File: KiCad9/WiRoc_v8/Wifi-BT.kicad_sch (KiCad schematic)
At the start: 1 part, among them U19 ESP32-C5-Board

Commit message: etc
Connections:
- net VDD_SYS_3.3V: now also U19.10 (VDD33); no longer U19.1 (VDD33)
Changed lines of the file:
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@@
-	)
-	(no_connect
-		(at 161.29 82.55)
 	)
 	(no_connect
 		(at 137.16 82.55)
+	)
+	(no_connect
+		(at 137.16 80.01)
 	)
 	(global_label "WIFI-SPI-CS0"
@@
 	(global_label "VDD_SYS_3.3V"
 		(shape input)
-		(at 137.16 80.01 180)
+		(at 161.29 82.55 0)
 		(fields_autoplaced yes)
 		(effects
@@
 				(size 1.524 1.524)
 			)
-			(justify right)
+			(justify left)
 		)
 		(property "Intersheetrefs" "${INTERSHEET_REFS}"
-			(at 118.5428 80.01 0)
+			(at 179.9072 82.55 0)
 			(effects
 				(font
 					(size 1.27 1.27)
 				)
-				(justify right)
+				(justify left)
 				(hide yes)
 			)

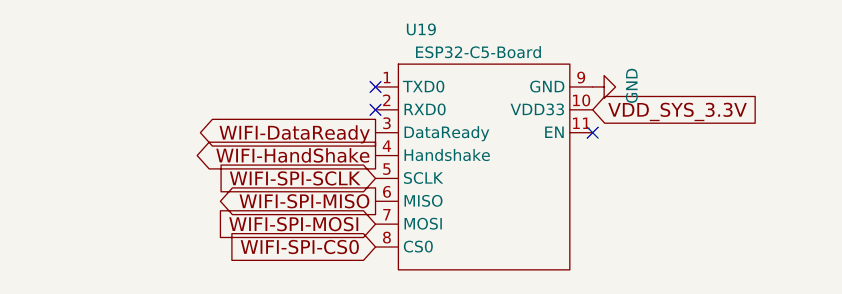
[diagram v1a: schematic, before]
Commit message: more routing of WiRoc_v8, upgraded USBConnectorPlate to v9 and with ferrit beads, added an ESPHosted testboard
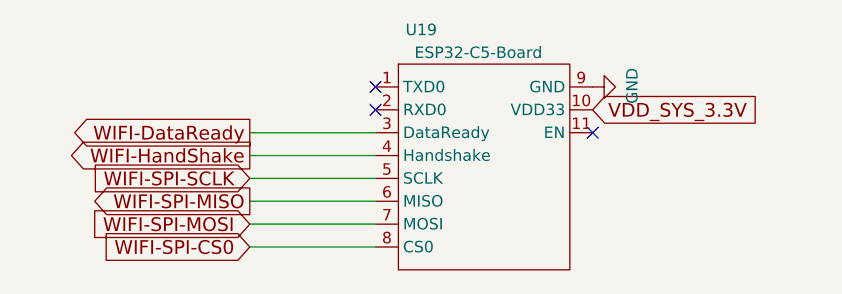
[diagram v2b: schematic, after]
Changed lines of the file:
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@@
 		(at 137.16 80.01)
 	)
+	(wire
+		(pts
+			(xy 123.19 92.71) (xy 137.16 92.71)
+		)
+		(stroke
+			(width 0)
+			(type default)
+		)
+	)
+	(wire
+		(pts
+			(xy 123.19 90.17) (xy 137.16 90.17)
+		)
+		(stroke
+			(width 0)
+			(type default)
+		)
+	)
+	(wire
+		(pts
+			(xy 123.19 87.63) (xy 137.16 87.63)
+		)
+		(stroke
+			(width 0)
+			(type default)
+		)
+	)
+	(wire
+		(pts
+			(xy 123.19 85.09) (xy 137.16 85.09)
+		)
+		(stroke
+			(width 0)
+			(type default)
+		)
+	)
+	(wire
+		(pts
+			(xy 123.19 97.79) (xy 137.16 97.79)
+		)
+		(stroke
+			(width 0)
+			(type default)
+		)
+	)
+	(wire
+		(pts
+			(xy 123.19 95.25) (xy 137.16 95.25)
+		)
+		(stroke
+			(width 0)
+			(type default)
+		)
+	)
 	(global_label "WIFI-SPI-CS0"
 		(shape input)
-		(at 137.16 97.79 180)
-		(fields_autoplaced yes)
-		(effects
-			(font
-				(size 1.524 1.524)
-			)
-			(justify right)
-		)
-		(property "Intersheetrefs" "${INTERSHEET_REFS}"
-			(at 117.9621 97.79 0)
+		(at 123.19 97.79 180)
+		(fields_autoplaced yes)
+		(effects
+			(font
+				(size 1.524 1.524)
+			)
+			(justify right)
+		)
+		(property "Intersheetrefs" "${INTERSHEET_REFS}"
+			(at 103.9921 97.79 0)
 			(effects
 				(font
@@
 	(global_label "WIFI-DataReady"
 		(shape output)
-		(at 137.16 85.09 180)
-		(fields_autoplaced yes)
-		(effects
-			(font
-				(size 1.524 1.524)
-			)
-			(justify right)
-		)
-		(property "Intersheetrefs" "${INTERSHEET_REFS}"
-			(at 116.075 85.09 0)
+		(at 123.19 85.09 180)
+		(fields_autoplaced yes)
+		(effects
+			(font
+				(size 1.524 1.524)
+			)
+			(justify right)
+		)
+		(property "Intersheetrefs" "${INTERSHEET_REFS}"
+			(at 102.105 85.09 0)
 			(effects
 				(font
@@
 	(global_label "WIFI-SPI-SCLK"
 		(shape input)
-		(at 137.16 90.17 180)
-		(fields_autoplaced yes)
-		(effects
-			(font
-				(size 1.524 1.524)
-			)
-			(justify right)
-		)
-		(property "Intersheetrefs" "${INTERSHEET_REFS}"
-			(at 116.6558 90.17 0)
+		(at 123.19 90.17 180)
+		(fields_autoplaced yes)
+		(effects
+			(font
+				(size 1.524 1.524)
+			)
+			(justify right)
+		)
+		(property "Intersheetrefs" "${INTERSHEET_REFS}"
+			(at 102.6858 90.17 0)
 			(effects
 				(font
@@
 	(global_label "WIFI-SPI-MISO"
 		(shape output)
-		(at 137.16 92.71 180)
-		(fields_autoplaced yes)
-		(effects
-			(font
-				(size 1.524 1.524)
-			)
-			(justify right)
-		)
-		(property "Intersheetrefs" "${INTERSHEET_REFS}"
-			(at 116.8735 92.71 0)
+		(at 123.19 92.71 180)
+		(fields_autoplaced yes)
+		(effects
+			(font
+				(size 1.524 1.524)
+			)
+			(justify right)
+		)
+		(property "Intersheetrefs" "${INTERSHEET_REFS}"
+			(at 102.9035 92.71 0)
 			(effects
 				(font
@@
 	(global_label "WIFI-HandShake"
 		(shape output)
-		(at 137.16 87.63 180)
-		(fields_autoplaced yes)
-		(effects
-			(font
-				(size 1.524 1.524)
-			)
-			(justify right)
-		)
-		(property "Intersheetrefs" "${INTERSHEET_REFS}"
-			(at 115.4944 87.63 0)
+		(at 123.19 87.63 180)
+		(fields_autoplaced yes)
+		(effects
+			(font
+				(size 1.524 1.524)
+			)
+			(justify right)
+		)
+		(property "Intersheetrefs" "${INTERSHEET_REFS}"
+			(at 101.5244 87.63 0)
 			(effects
 				(font
@@
 	(global_label "WIFI-SPI-MOSI"
 		(shape input)
-		(at 137.16 95.25 180)
-		(fields_autoplaced yes)
-		(effects
-			(font
-				(size 1.524 1.524)
-			)
-			(justify right)
-		)
-		(property "Intersheetrefs" "${INTERSHEET_REFS}"
-			(at 116.8735 95.25 0)
-			(effects
-				(font
-					(size 1.27 1.27)
-				)
-				(justify right)
-				(hide yes)
-			)
-		)
+		(at 123.19 95.25 180)
+		(fields_autoplaced yes)
+		(effects
+			(font
+				(size 1.524 1.524)
+			)
+			(justify right)
+		)
+		(property "Intersheetrefs" "${INTERSHEET_REFS}"
+			(at 102.9035 95.25 0)
+			(effects
+				(font
+					(size 1.27 1.27)
+				)
+				(justify right)
+				(hide yes)
+			)
+		)
+	)
+	(rule_area
+		(polyline
+			(pts
+				(xy 125.73 100.965) (xy 125.73 81.28) (xy 128.27 81.28) (xy 128.27 100.965)
+			)
+			(stroke
+				(width 0)
+				(type dash)
+			)
+			(fill
+				(type none)
+			)
+		)
+	)
+	(netclass_flag ""
+		(length 2.54)
+		(shape round)
+		(at 127 81.28 0)
+		(fields_autoplaced yes)
+		(effects
+			(font
+				(size 1.524 1.524)
+			)
+			(justify left bottom)
+		)
+		(property "Netclass" "WIFI"
+			(at 127.6299 78.74 0)
+			(effects
+				(font
+					(size 1.27 1.27)
+				)
+				(justify left)
+			)
+		)
+		(property "Component Class" ""
+			(at -69.85 -2.54 0)
+			(effects
+				(font
+					(size 1.27 1.27)
+					(italic yes)
+				)
+			)
+		)

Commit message: add bom
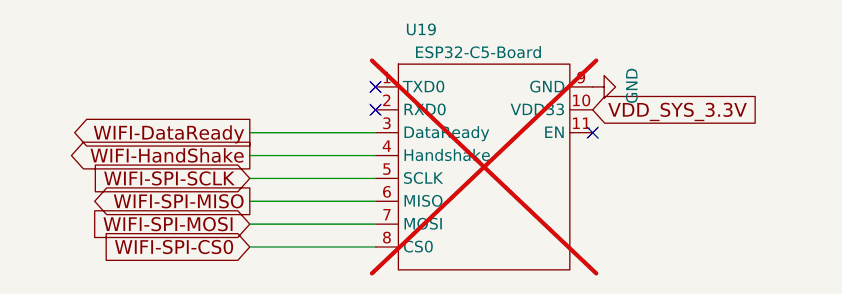
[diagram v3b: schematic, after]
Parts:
- U19: IncludeInBOM (none) -> FALSE; now not fitted
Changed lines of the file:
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@@
 		(in_bom yes)
 		(on_board yes)
-		(dnp no)
+		(dnp yes)
 		(property "Reference" "U19"
 			(at 142.24 73.66 0)
@@
 			(at 149.86 88.9 0)
 			(effects
+				(font
+					(size 1.27 1.27)
+				)
+				(hide yes)
+			)
+		)
+		(property "JLCBasicExtended" ""
+			(at 149.86 88.9 0)
+			(effects
+				(font
+					(size 1.27 1.27)
+				)
+				(hide yes)
+			)
+		)
+		(property "IncludeInBOM" "FALSE"
+			(at 149.86 88.9 0)
+			(effects

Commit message: add rst to wifi board
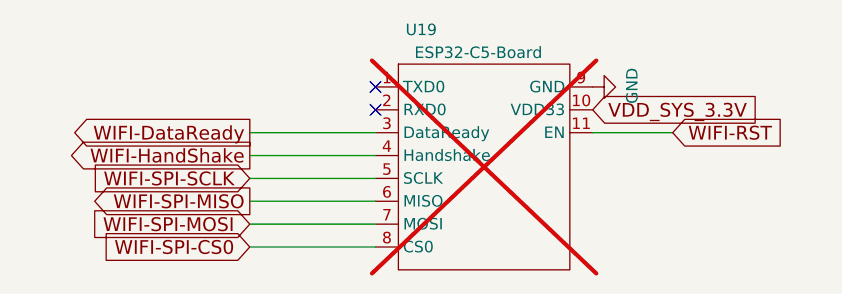
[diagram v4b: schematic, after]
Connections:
- net WIFI-RST: now reaches U19.11 (EN)
- no-connect marks 3 -> 2
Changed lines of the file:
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@@
 	(paper "A4")
 	(no_connect
-		(at 161.29 85.09)
-	)
-	(no_connect
 		(at 137.16 82.55)
 	)
 	(no_connect
 		(at 137.16 80.01)
+	)
+	(wire
+		(pts
+			(xy 170.18 85.09) (xy 161.29 85.09)
+		)
+		(stroke
+			(width 0)
+			(type default)
+		)
 	)
 	(wire
@@
 				)
 				(justify right)
+				(hide yes)
+			)
+		)
+	)
+	(global_label "WIFI-RST"
+		(shape input)
+		(at 170.18 85.09 0)
+		(fields_autoplaced yes)
+		(effects
+			(font
+				(size 1.524 1.524)
+			)
+			(justify left)
+		)
+		(property "Intersheetrefs" "${INTERSHEET_REFS}"
+			(at 183.4996 85.09 0)
+			(effects
+				(font
+					(size 1.27 1.27)
+				)
+				(justify left)
 				(hide yes)
 			)
@@
 			)
 		)
+	)
+	(netclass_flag ""
+		(length 2.54)
+		(shape round)
+		(at 166.37 85.09 180)
+		(fields_autoplaced yes)
+		(effects
+			(font
+				(size 1.524 1.524)
+			)
+			(justify right bottom)
+		)
+		(property "Netclass" "WIFI"
+			(at 166.9999 87.63 0)
+			(effects
+				(font
+					(size 1.27 1.27)
+				)
+				(justify left)
+			)
+		)
+		(property "Component Class" ""
+			(at -66.04 -6.35 0)
+			(effects
+				(font
+					(size 1.27 1.27)
+					(italic yes)
+				)
+			)
+		)

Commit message: add esp32hosted-c5 board
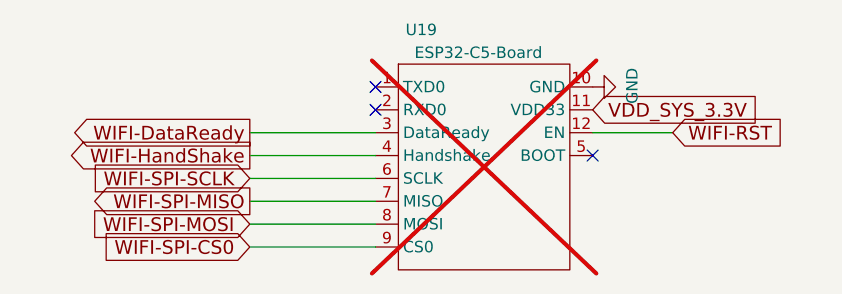
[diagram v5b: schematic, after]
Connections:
- net GND: now also U19.10 (GND); no longer U19.9 (GND)
- net VDD_SYS_3.3V: now also U19.11 (VDD33); no longer U19.10 (VDD33)
- net WIFI-RST: now also U19.12 (EN); no longer U19.11 (EN)
- net WIFI-SPI-CS0: now also U19.9 (CS0); no longer U19.8 (CS0)
- net WIFI-SPI-MISO: now also U19.7 (MISO); no longer U19.6 (MISO)
- net WIFI-SPI-MOSI: now also U19.8 (MOSI); no longer U19.7 (MOSI)
- net WIFI-SPI-SCLK: now also U19.6 (SCLK); no longer U19.5 (SCLK)
- no-connect marks 2 -> 3
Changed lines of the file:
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@@
+	)
+	(no_connect
+		(at 161.29 87.63)
 	)
 	(no_connect
@@
 		(pin "1"
 		)
+		(pin "12"
+		)
 		(instances

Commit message: etc
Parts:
- U19: now left out of the parts list
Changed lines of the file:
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@@
 		(unit 1)
 		(exclude_from_sim no)
-		(in_bom yes)
+		(in_bom no)
 		(on_board yes)
 		(dnp yes)
